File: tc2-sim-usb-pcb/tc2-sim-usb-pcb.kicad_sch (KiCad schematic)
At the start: 9 parts, among them J11 Conn_01x08

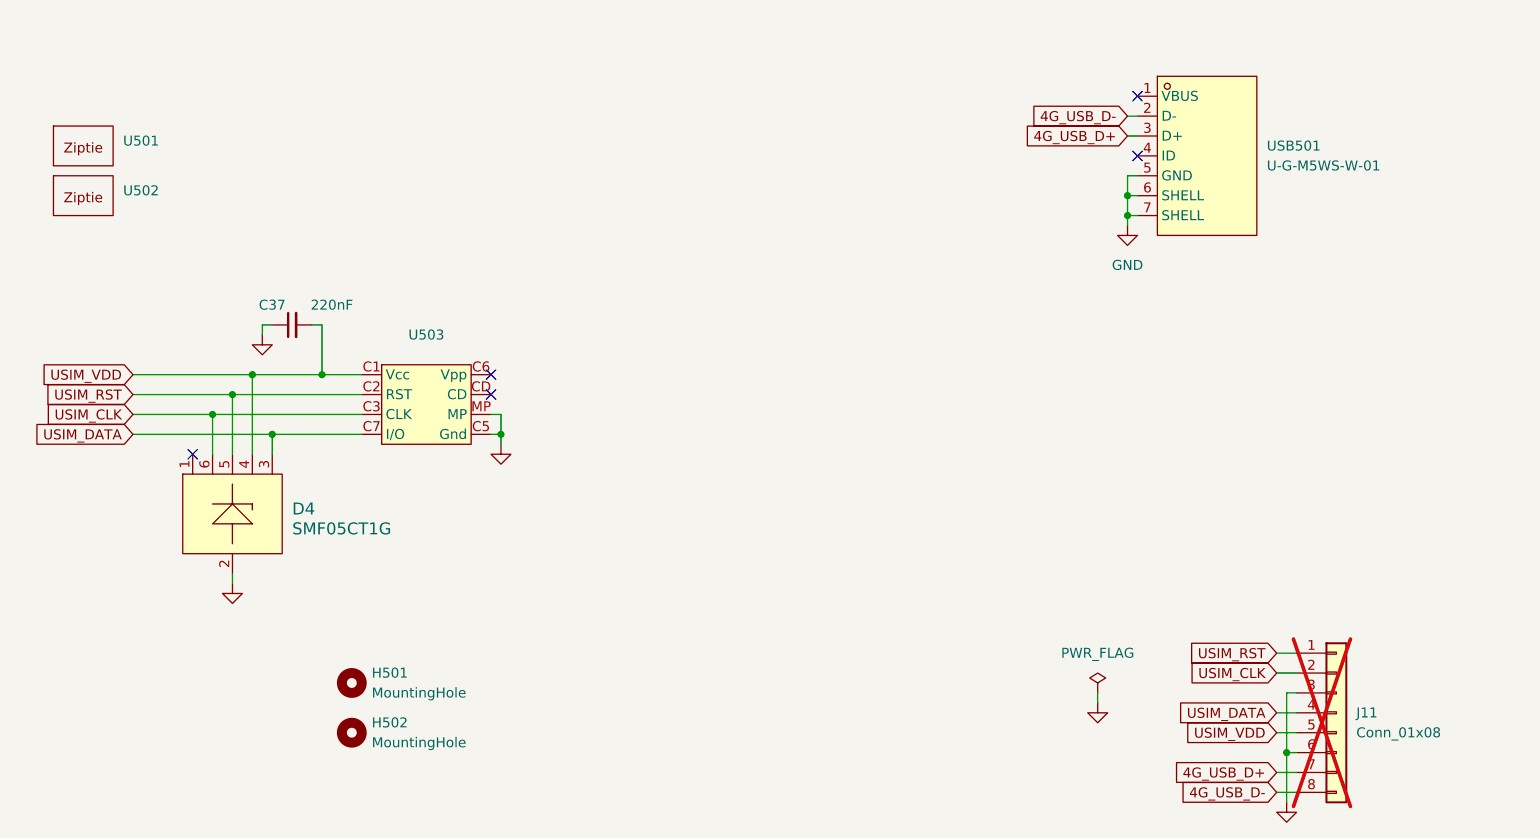
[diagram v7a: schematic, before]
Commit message: Update to kicad 9, fix microphone panel v cuts
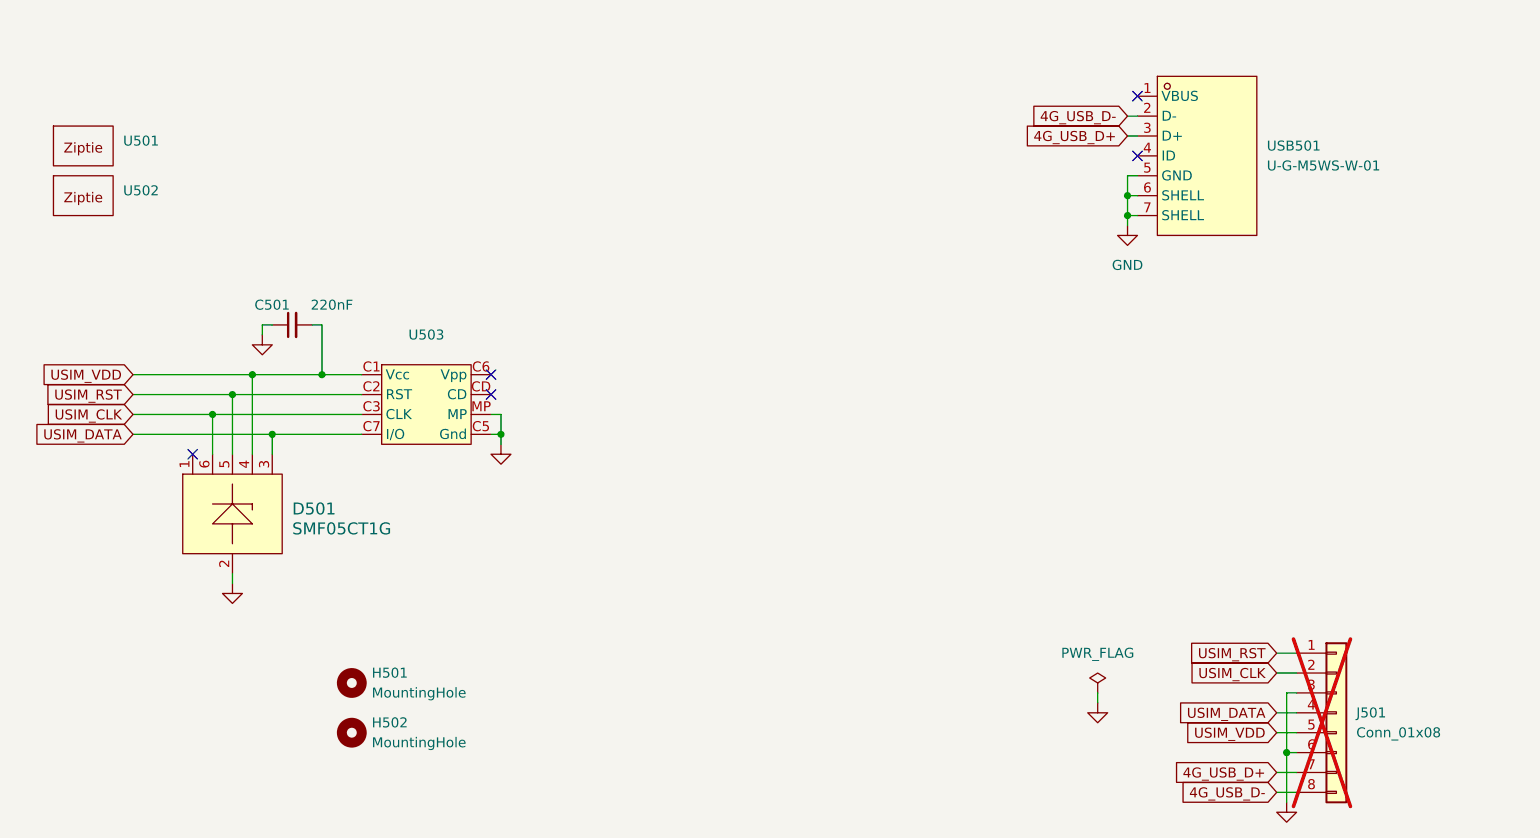
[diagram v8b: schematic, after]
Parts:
- renumbered C37 to C501, D4 to D501, J11 to J501
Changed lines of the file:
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@@
 (kicad_sch
-	(version 20231120)
+	(version 20250114)
 	(generator "eeschema")
-	(generator_version "8.0")
+	(generator_version "9.0")
 	(paper "A4")
 	(junction
@@
 		(dnp no)
 		(fields_autoplaced yes)
-		(property "Reference" "D4"
+		(property "Reference" "D501"
 			(at 102.87 104.775 0)
 			(effects
@@
 		(dnp no)
 		(fields_autoplaced yes)
-		(property "Reference" "#PWR076"
+		(property "Reference" "#PWR0502"
 			(at 99.06 88.9 0)
 			(effects
@@
 		(dnp yes)
 		(fields_autoplaced yes)
-		(property "Reference" "J11"
+		(property "Reference" "J501"
 			(at 238.76 130.81 0)
 			(effects
@@
 		(dnp no)
 		(fields_autoplaced yes)
-		(property "Reference" "#PWR077"
+		(property "Reference" "#PWR0504"
 			(at 95.25 120.65 0)
 			(effects
@@
 		(dnp no)
 		(fields_autoplaced yes)
-		(property "Reference" "#PWR077"
+		(property "Reference" "#PWR0503"
 			(at 129.54 102.87 0)
 			(effects
@@
 		(on_board yes)
 		(dnp no)
-		(property "Reference" "C37"
+		(property "Reference" "C501"
 			(at 100.33 78.74 90)
 			(effects
@@
 		(dnp no)
 		(fields_autoplaced yes)
-		(property "Reference" "#PWR079"
+		(property "Reference" "#PWR0506"
 			(at 229.87 148.59 0)
 			(effects
@@
 		)
 	)
+	(embedded_fonts no)
 )
